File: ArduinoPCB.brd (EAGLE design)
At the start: 100 x 80 mm, 19 parts, among them T1 2N4923

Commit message: Updated PCB
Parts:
- removed D1: (no value), diode:P1Z12
- removed R2: (no value), rcl:0309/12
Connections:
- removed net N$15: D1.C, R2.1, T1.3
- net N$16: no longer R2.2
- net N$8: now also T1.3; no longer D1.A
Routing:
- net N$15: track 32.4 -> 0.00 mm
- net N$8: track 203.7 -> 234.0 mm
- net N$16: track 23.7 -> 25.2 mm
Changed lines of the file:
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@@
 <attribute name="VALUE" x="11.049" y="27.432" size="1.27" layer="27" ratio="10" rot="R270"/>
-</element>
-<element name="D1" library="diode" library_urn="urn:adsk.eagle:library:210" package="P1Z12" package3d_urn="urn:adsk.eagle:package:43340/1" value="" x="81.28" y="31.75" smashed="yes" rot="R180">
-<attribute name="NAME" x="84.328" y="29.972" size="1.27" layer="25" ratio="10" rot="R180"/>
-<attribute name="POPULARITY" value="1" x="59.69" y="114.3" size="1.778" layer="27" rot="R180" display="off"/>
-<attribute name="VALUE" x="84.328" y="34.925" size="1.27" layer="27" ratio="10" rot="R180"/>
 </element>
 <element name="FRAME1" library="SparkFun-Aesthetics" library_urn="urn:adsk.eagle:library:507" package="CREATIVE_COMMONS" package3d_urn="urn:adsk.eagle:package:37121/1" value="FRAME-LETTER" x="-80.01" y="66.04" smashed="yes"/>
@@
 <attribute name="SPICEPREFIX" value="R" x="140.97" y="71.12" size="1.778" layer="27" rot="R90" display="off"/>
 <attribute name="VALUE" x="65.4558" y="47.625" size="1.27" layer="27" ratio="10" rot="R90"/>
-</element>
-<element name="R2" library="rcl" library_urn="urn:adsk.eagle:library:334" package="0309/12" package3d_urn="urn:adsk.eagle:package:23571/1" value="" x="78.74" y="43.18" smashed="yes" rot="R90">
-<attribute name="NAME" x="76.835" y="38.989" size="1.27" layer="25" ratio="10" rot="R90"/>
-<attribute name="POPULARITY" value="8" x="154.94" y="78.74" size="1.778" layer="27" rot="R90" display="off"/>
-<attribute name="SPICEPREFIX" value="R" x="154.94" y="78.74" size="1.778" layer="27" rot="R90" display="off"/>
-<attribute name="VALUE" x="79.4258" y="40.005" size="1.27" layer="27" ratio="10" rot="R90"/>
 </element>
 <element name="R3" library="rcl" library_urn="urn:adsk.eagle:library:334" package="0309/12" package3d_urn="urn:adsk.eagle:package:23571/1" value="" x="52.07" y="50.8" smashed="yes" rot="R90">
@@
 <wire x1="25.4508" y1="51.9684" x2="25.4" y2="52.07" width="0.1524" layer="1"/>
 </signal>
-<signal name="N$15">
-<contactref element="R2" pad="1"/>
-<contactref element="D1" pad="C"/>
-<contactref element="T1" pad="3"/>
-<wire x1="82.7532" y1="36.7284" x2="78.7908" y2="36.7284" width="0.1524" layer="16"/>
-<wire x1="87.63" y1="31.8516" x2="82.7532" y2="36.7284" width="0.1524" layer="16"/>
-<wire x1="78.7908" y1="36.7284" x2="78.74" y2="36.83" width="0.1524" layer="16"/>
-<wire x1="87.63" y1="31.8516" x2="87.63" y2="31.75" width="0.1524" layer="16"/>
-<wire x1="84.7344" y1="38.7096" x2="84.7344" y2="57.15" width="0.1524" layer="16"/>
-<wire x1="82.7532" y1="36.7284" x2="84.7344" y2="38.7096" width="0.1524" layer="16"/>
-<wire x1="84.7344" y1="57.15" x2="84.836" y2="57.15" width="0.1524" layer="16"/>
-</signal>
 <signal name="N$16">
-<contactref element="R2" pad="2"/>
 <contactref element="S6" pad="2"/>
 <contactref element="T1" pad="2"/>
-<wire x1="78.6384" y1="49.53" x2="68.58" y2="39.4716" width="0.1524" layer="1"/>
-<wire x1="68.58" y1="39.4716" x2="68.58" y2="39.37" width="0.1524" layer="1"/>
-<wire x1="78.6384" y1="49.53" x2="78.74" y2="49.53" width="0.1524" layer="1"/>
-<wire x1="82.4484" y1="53.1876" x2="82.4484" y2="57.15" width="0.1524" layer="16"/>
-<wire x1="78.7908" y1="49.53" x2="82.4484" y2="53.1876" width="0.1524" layer="16"/>
+<wire x1="82.4484" y1="50.4952" x2="71.3232" y2="39.37" width="0.1524" layer="16"/>
+<wire x1="68.58" y1="39.37" x2="71.3232" y2="39.37" width="0.1524" layer="16"/>
+<wire x1="82.4484" y1="57.15" x2="82.4484" y2="50.4952" width="0.1524" layer="16"/>
 <wire x1="82.4484" y1="57.15" x2="82.55" y2="57.15" width="0.1524" layer="16"/>
-<wire x1="78.7908" y1="49.53" x2="78.74" y2="49.53" width="0.1524" layer="16"/>
 </signal>
 <signal name="N$8">
-<wire x1="83.82" y1="35.56" x2="74.93" y2="35.56" width="0.1524" layer="1"/>
-<contactref element="D1" pad="A"/>
 <contactref element="G1" pad="-"/>
 <contactref element="U$1" pad="GND"/>
@@
 <contactref element="LEDENGINE" pad="K"/>
 <contactref element="LEDEXT" pad="K"/>
-<wire x1="74.93" y1="35.56" x2="74.93" y2="35.5092" width="0.1524" layer="1"/>
-<wire x1="74.93" y1="35.5092" x2="74.93" y2="31.75" width="0.1524" layer="1"/>
-<wire x1="78.6384" y1="28.0416" x2="78.6384" y2="17.8308" width="0.1524" layer="16"/>
+<wire x1="78.6384" y1="29.1592" x2="78.6384" y2="17.8308" width="0.1524" layer="16"/>
 <wire x1="78.6384" y1="17.8308" x2="78.6384" y2="14.0208" width="0.1524" layer="16"/>
-<wire x1="74.93" y1="31.75" x2="78.6384" y2="28.0416" width="0.1524" layer="16"/>
 <wire x1="78.6384" y1="14.0208" x2="78.74" y2="13.97" width="0.1524" layer="16"/>
 <wire x1="78.6384" y1="17.8308" x2="39.4716" y2="17.8308" width="0.1524" layer="16"/>
@@
 <wire x1="39.37" y1="57.15" x2="52.07" y2="57.15" width="0.1524" layer="1"/>
 <wire x1="52.07" y1="57.15" x2="64.77" y2="57.15" width="0.1524" layer="1"/>
-<wire x1="70.4088" y1="35.5092" x2="74.93" y2="35.5092" width="0.1524" layer="1"/>
-<wire x1="65.6844" y1="40.2336" x2="70.4088" y2="35.5092" width="0.1524" layer="1"/>
-<wire x1="65.6844" y1="56.2356" x2="65.6844" y2="40.2336" width="0.1524" layer="1"/>
-<wire x1="64.77" y1="57.15" x2="65.6844" y2="56.2356" width="0.1524" layer="1"/>
-<wire x1="74.9808" y1="35.5092" x2="74.93" y2="35.5092" width="0.1524" layer="1"/>
+<wire x1="67.818" y1="35.56" x2="81.3308" y2="35.56" width="0.1524" layer="1"/>
+<wire x1="66.9544" y1="36.4236" x2="67.818" y2="35.56" width="0.1524" layer="1"/>
+<wire x1="66.9544" y1="54.9656" x2="66.9544" y2="36.4236" width="0.1524" layer="1"/>
+<wire x1="64.77" y1="57.15" x2="66.9544" y2="54.9656" width="0.1524" layer="1"/>
 <contactref element="LEDINFO1" pad="K"/>
-<wire x1="87.63" y1="39.3192" x2="91.44" y2="39.3192" width="0.1524" layer="1"/>
-<wire x1="83.82" y1="35.5092" x2="87.63" y2="39.3192" width="0.1524" layer="1"/>
+<wire x1="85.09" y1="39.3192" x2="91.44" y2="39.3192" width="0.1524" layer="1"/>
+<wire x1="81.3308" y1="35.56" x2="85.09" y2="39.3192" width="0.1524" layer="1"/>
 <wire x1="91.44" y1="39.3192" x2="91.44" y2="39.37" width="0.1524" layer="1"/>
-<wire x1="83.82" y1="35.5092" x2="83.82" y2="35.56" width="0.1524" layer="1"/>
+<contactref element="T1" pad="3"/>
+<wire x1="84.8868" y1="46.0248" x2="84.8868" y2="57.15" width="0.1524" layer="16"/>
+<wire x1="91.44" y1="39.4716" x2="90.1954" y2="40.7162" width="0.1524" layer="16"/>
+<wire x1="90.1954" y1="40.7162" x2="84.8868" y2="46.0248" width="0.1524" layer="16"/>
+<wire x1="84.8868" y1="57.15" x2="84.836" y2="57.15" width="0.1524" layer="16"/>
+<wire x1="91.44" y1="39.4716" x2="91.44" y2="39.37" width="0.1524" layer="16"/>
+<wire x1="78.6384" y1="29.1592" x2="90.1954" y2="40.7162" width="0.1524" layer="16"/>
 </signal>
 <signal name="N$5">
@@
 <mfgpreviewcolor name="substratecolor" color="0xFF786E46"/>
 </mfgpreviewcolors>
-<errors>
-</errors>
 </board>
 </drawing>

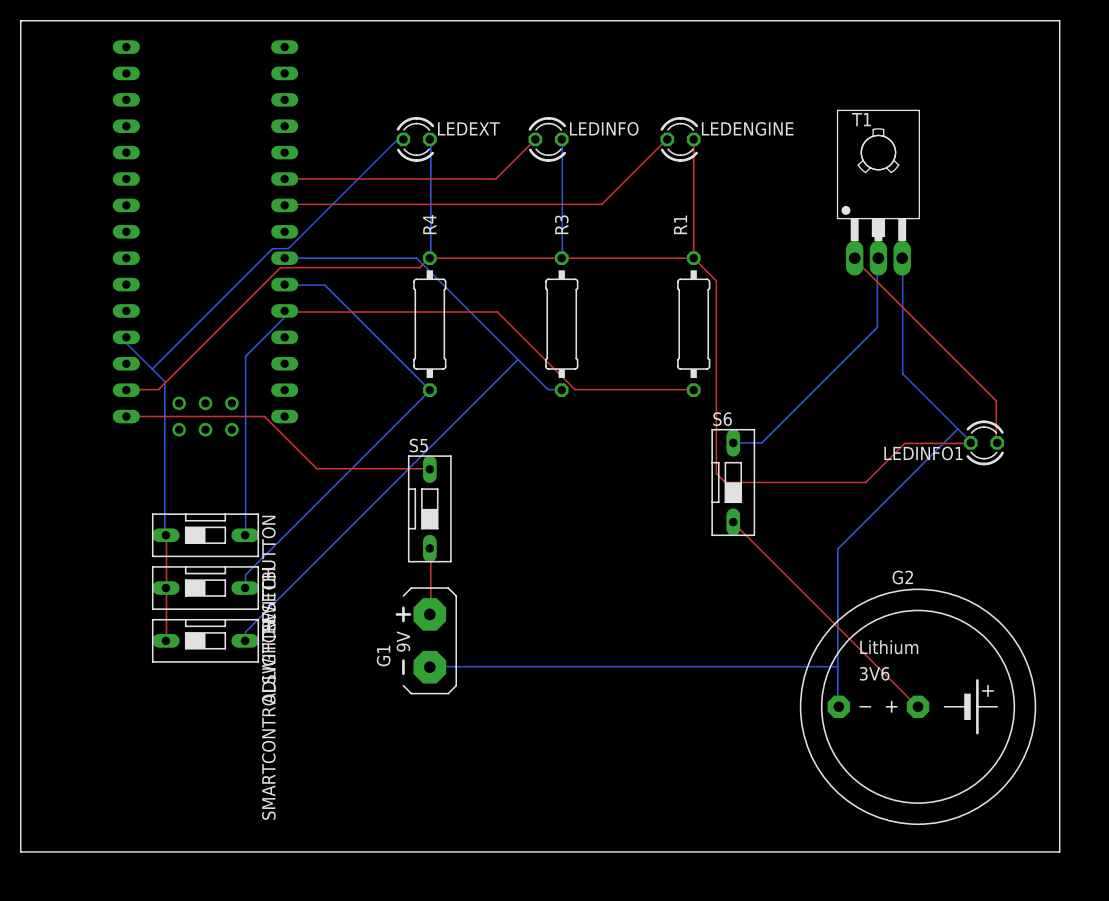
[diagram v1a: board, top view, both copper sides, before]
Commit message: thicker lines
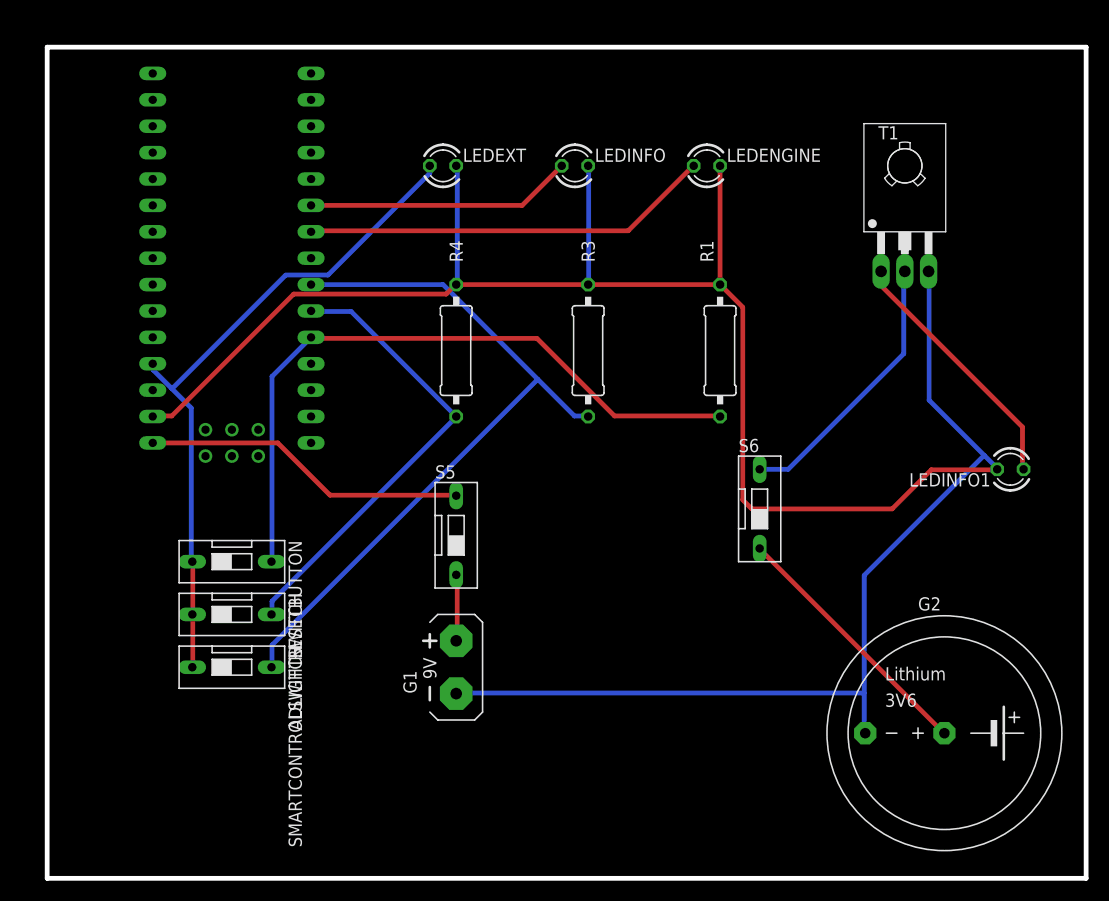
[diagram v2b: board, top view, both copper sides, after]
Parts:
- moved FRAME1 3.59 mm to (-77.5, 63.5)
- moved G2 3.59 mm to (88.9, 11.4)
- moved LEDINFO1 3.59 mm to (95.2, 36.8)
- moved R1 3.59 mm to (67.3, 48.3)
- moved S6 3.59 mm to (71.1, 33.0)
- moved S5 3.59 mm to (41.9, 30.5)
- moved ADLIGHTSWITCH 3.59 mm to (20.3, 22.9)
- moved G1 3.59 mm to (41.9, 17.8)
- moved LEDENGINE 3.59 mm to (66.0, 66.0)
- moved LEDINFO 3.59 mm to (53.3, 66.0)
- moved R3 3.59 mm to (54.6, 48.3)
- moved R4 3.59 mm to (41.9, 48.3)
- moved RESETBUTTON 3.59 mm to (20.3, 27.9)
- moved SMARTCONTROLSWITCH 3.59 mm to (20.3, 17.8)
- moved U$1 3.59 mm to (22.9, 48.3)
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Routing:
- net N$16: track 25.2 -> 26.5 mm
- net N$8: track 234.0 -> 235.2 mm
- net N$5: track 23.6 -> 24.8 mm
- net N$9: track 64.3 -> 65.1 mm
